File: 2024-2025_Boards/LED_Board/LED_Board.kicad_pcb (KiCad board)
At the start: 2 copper layers, 60 x 37.5 mm, 70 parts, among them J1 Conn_02x10_Odd_Even, J10 Conn_01x03_Pin, J11 Conn_01x03_Pin, J2 Conn_01x02_Pin, J3 Conn_01x02_Pin, J4 Conn_ARM_JTAG_SWD_10, J5 Conn_01x05_Pin, J6 Conn_01x03_Pin, J7 Conn_01x03_Pin, J8 Conn_01x03_Pin, J9 Conn_01x03_Pin, U1 TLVM23625RDNR, U2 AMS1117-3.3, U3 STM32G431CBT6, U4 TCAN1057AEV-Q1, U5 CSD88537ND, U6 CSD88537ND

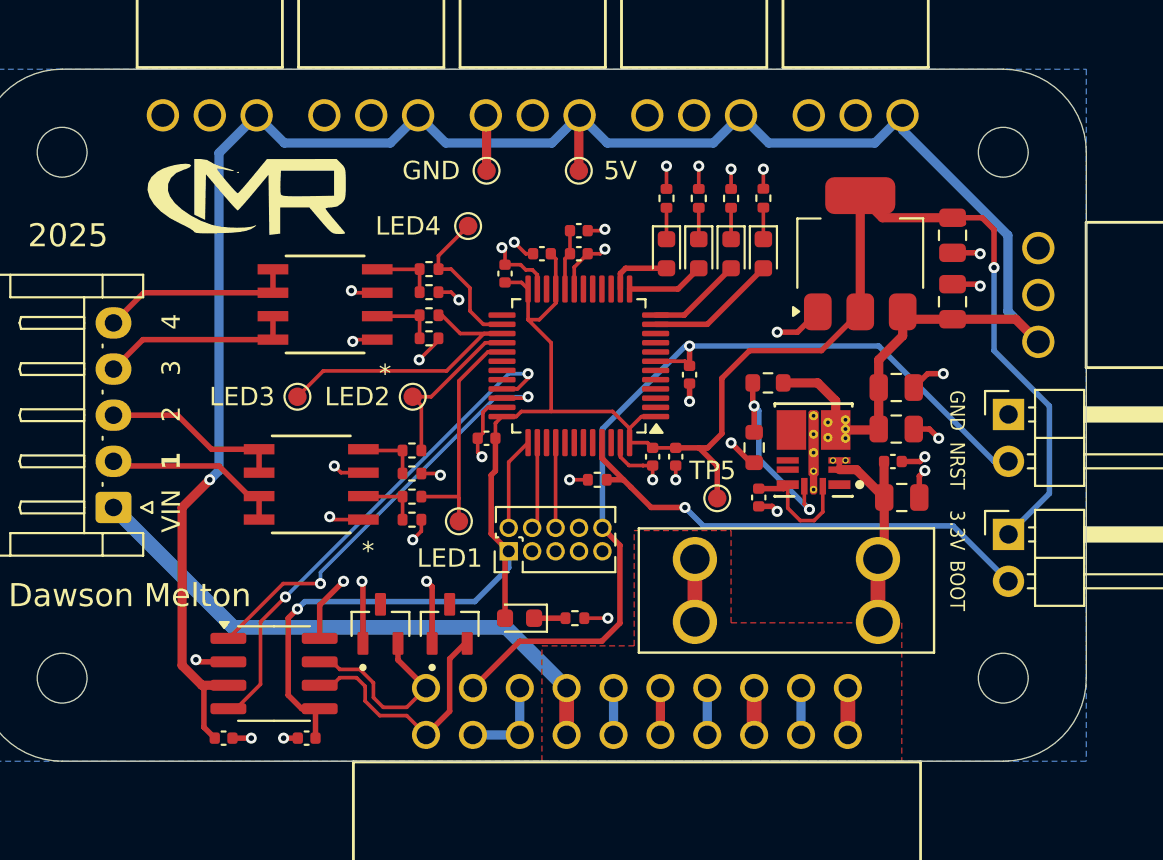
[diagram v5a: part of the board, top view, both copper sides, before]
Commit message: LED Board Finished
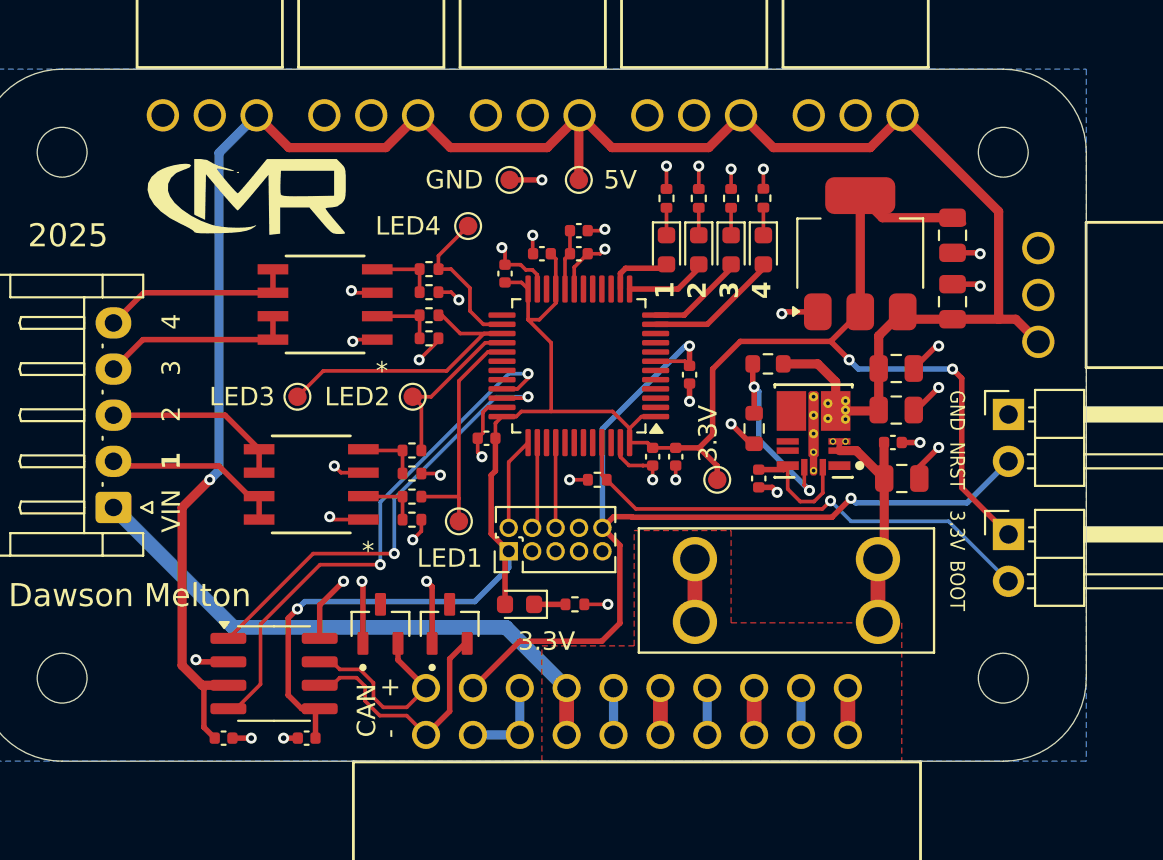
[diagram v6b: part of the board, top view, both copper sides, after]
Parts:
- moved GND 1.35 mm to (118.8, 118.5)
- moved C1 1.03 mm to (140.0, 134.7)
- moved C2 1.03 mm to (139.5, 132.7)
- moved C3 1.03 mm to (139.7, 128.7)
- moved C4 1.03 mm to (139.7, 131.0)
- moved C5 1.03 mm to (132.3, 134.7)
- moved R1 1.03 mm to (132.8, 128.5)
- moved R2 1.03 mm to (132.0, 132.0)
- moved U1 1.03 mm to (135.2, 132.0)
- moved 3.3V 1.00 mm to (130.0, 134.8)
- moved D3 0.75 mm to (119.3, 141.5)
- moved R12 0.75 mm to (122.3, 141.5)
- moved 5V 0.50 mm to (122.5, 118.5)
- moved D4 0.21 mm to (127.2, 122.3)
- moved D5 0.21 mm to (129.0, 122.3)
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- renumbered TP5 to 3.3V
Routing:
- net 3.3V: track 111.1 -> 105.7 mm, vias 2 -> 3
- net NRST: track 49.8 -> 53.7 mm, vias 1 -> 2
- net CAN_RX: track 27.6 -> 29.6 mm
- net 5V: track 120.2 -> 118.4 mm
- net GND: track 82.2 -> 80.5 mm, vias 37 -> 38
- net CAN_TX: track 23.5 -> 24.9 mm
- net V_Fuse: track 12.4 -> 13.4 mm
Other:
- board text added: "+"
- board text added: "-"
- board text added: "CAN"

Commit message: Board fixes
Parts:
- added D8: YELLOW, LED_SMD:LED_0603_1608Metric, F.Cu at (100.0, 141.8)
- added D9: YELLOW, LED_SMD:LED_0603_1608Metric, F.Cu at (143.8, 138.8)
- added R17: 2k, Resistor_SMD:R_0402_1005Metric, F.Cu at (100.0, 145.0)
- added R18: 10k, Resistor_SMD:R_0402_1005Metric, F.Cu at (143.8, 142.0)
- C14, C15: footprint Capacitor_SMD:C_0402_1005Metric -> Capacitor_SMD:C_0603_1608Metric
- D3: value RED -> YELLOW
- TP1: renamed from GND; value TestPoint -> GND
- TP2: renamed from LED1; value TestPoint -> LED1
- TP3: renamed from 5V; value TestPoint -> 5V
- TP4: renamed from LED2; value TestPoint -> LED2
- TP5: renamed from 3.3V; value TestPoint -> 3.3V
- TP6: renamed from LED3; value TestPoint -> LED3
- TP7: renamed from LED4; value TestPoint -> LED4
- moved H3 4.60 mm to (148.8, 113.8)
- moved J3 4.02 mm to (149.1, 129.0)
- moved J2 3.66 mm to (149.1, 136.2)
- moved G*** 3.31 mm to (107.8, 120.2)
- moved H1 3.25 mm to (94.5, 113.8)
- moved H4 3.25 mm to (148.8, 145.5)
- moved TP5 3.00 mm to (130.0, 131.8)
- moved J6 2.99 mm to (147.5, 124.3)
- moved C11 1.75 mm to (128.2, 133.5)
- moved TP7 1.58 mm to (115.0, 121.5)
- moved C14 1.12 mm to (126.8, 134.0)
- moved C15 1.00 mm to (120.5, 121.5), turned to 90 degrees
- moved D1 0.37 mm to (111.8, 142.2)
- moved D2 0.31 mm to (115.5, 142.2)
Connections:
- J5 pad 1: V_IN -> V_Fuse
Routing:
- net V_Fuse: track 13.4 -> 67.5 mm
- net V_IN: track 42.2 -> 13.6 mm
- net NRST: track 53.7 -> 61.0 mm
- net BOOT0: track 26.5 -> 29.3 mm
- net 3.3V: track 105.7 -> 103.2 mm
- net GND: track 80.5 -> 78.4 mm, vias 38 -> 40
- net Net-(D9-K): track 0.00 -> 1.95 mm
- net Net-(D8-K): track 0.00 -> 1.92 mm
- net G4: track 8.67 -> 7.55 mm
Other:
- board size 60 x 37.5 mm -> 63.2 x 40.7 mm
- board text added: "5V"
- board text added: "LED1"
- board text added: "LED2"
- board text added: "LED3"
- board text added: "LED4"
- board text added: "PWR"
